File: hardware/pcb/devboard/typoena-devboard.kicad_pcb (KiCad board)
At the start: 4 copper layers, 117 x 45 mm, 86 parts, among them J1 BATTERIE JST-PH, J10 EXTENSION (non monte), J11 DEVKITC-1 rangée gauche, J12 DEVKITC-1 rangée droite, J13 CLAVIER INTERNE, J2 BOUTON contact JST-PH, J3 BOUTON LED JST-PH, J4 FPC 24p 0.5mm - PANNEAU, J5 SECOURS DESPI-C579, J6 USB-C CHARGE + PROG, J7 USB-C CLAVIER (hote), J8 microSD, Q1 AO3401A, Q2 2N7002, Q3 2N7002, Q4 Si1308EDL, SW1 QON, U2 BQ25896RTW, U3 TPS63001DRCR, U4 TPS61023DRL

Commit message: feat(pcb): ready the dev board for fabrication
- drop J10, the unpopulated extension header (schematic + copper)
- extend the In2.Cu +3V3 plane to the left board edge, closing the
  gap under the DevKitC headers, and refill the zones
- mark J11/J12 (DevKitC header rows) DNP for hand-soldering; give J13
  (internal-keyboard JST-PH S4B-PH-K) its LCSC C157926 for fab assembly
- add the dev board BOM source
- gen_fab: apply J13's +180 JLCPCB rotation, matching the other JST-PH
- check_pcb: treat an absent USB pair as not-present, not "unrouted"
  (USB_PROG only exists on the mainboard)

Co-Authored-By: Claude Opus 4.8 <noreply@anthropic.com>
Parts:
- removed J10: EXTENSION (non monte), Connector_PinHeader_2.54mm:PinHeader_1x12_P2.54mm_Vertical
- moved C16 10.5 mm to (23.3, 69.0), turned to 90 degrees
- moved C17 9.12 mm to (21.3, 69.0), turned to 90 degrees
- moved C15 4.60 mm to (22.4, 71.3)
- moved J11 0.40 mm to (19.5, 74.0)
- moved J12 0.40 mm to (19.5, 51.1)
- moved C30 0.30 mm to (33.4, 82.6)
- moved C9 0.30 mm to (36.1, 82.6)
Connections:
- J11 pad 12: IO8 -> unconnected-(J11-Pin_12-Pad12)
- J11 pad 15: IO9 -> unconnected-(J11-Pin_15-Pad15)
- J12 pad 16: IO48 -> unconnected-(J12-Pin_16-Pad16)
- J12 pad 17: IO47 -> unconnected-(J12-Pin_17-Pad17)
- J12 pad 4: IO1 -> unconnected-(J12-Pin_4-Pad4)
- J12 pad 5: IO2 -> unconnected-(J12-Pin_5-Pad5)
- J12 pad 6: IO42 -> unconnected-(J12-Pin_6-Pad6)
- J12 pad 9: IO39 -> unconnected-(J12-Pin_9-Pad9)
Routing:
- net USB_DP: track 5.52 -> 72.3 mm, vias 2 -> 4
- net USB_DM: track 4.29 -> 63.6 mm, vias 2 -> 4
- net SD_SCK: track 1.04 -> 47.6 mm
- net +5V: track 15.9 -> 61.3 mm, vias 4 -> 5
- net SD_MISO: track 6.27 -> 48.9 mm, vias 0 -> 1
- net VBAT: track 4.05 -> 18.0 mm, vias 0 -> 1
- net +3V3: track 47.4 -> 43.5 mm, vias 9 -> 8
- net SD_CS: track 59.8 -> 61.0 mm
- net VSYS: track 119.8 -> 121.0 mm, vias 1 -> 0
- net GND: track 59.0 -> 60.1 mm
- net EPD_SCK: track 102.0 -> 101.0 mm
- net PMIC_INT: track 56.4 -> 55.4 mm
- net EPD_MOSI: track 104.4 -> 103.4 mm
- net SD_MOSI: track 78.7 -> 79.3 mm
- net I2C_SCL: track 52.9 -> 52.4 mm

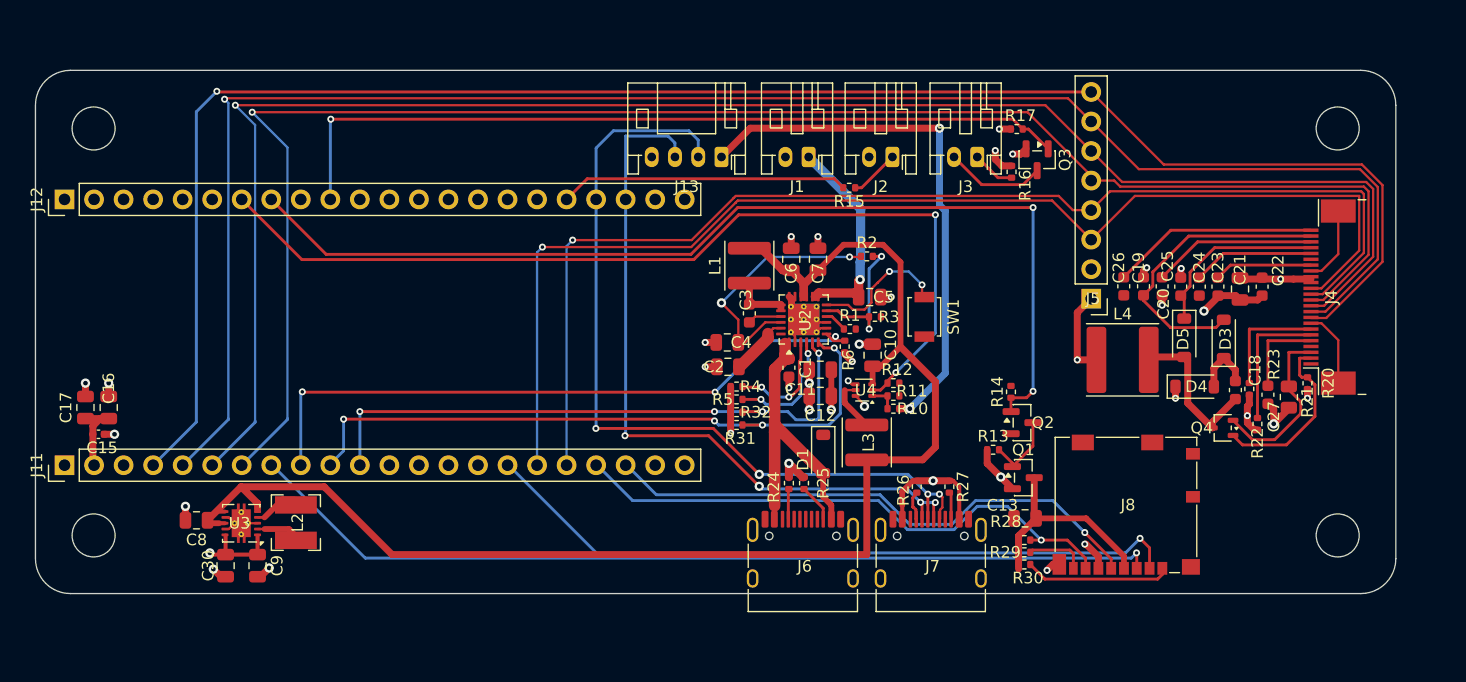
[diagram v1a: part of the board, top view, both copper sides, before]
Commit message: feat(pcb): cost-optimize the dev board for JLCPCB
- shrink the outline to 99 x 45 mm and recenter MH2/MH4, keeping every
  dimension under 100 mm to dodge the large-board engineering fee
- reshape the In2.Cu +5V plane, restore the GND_surface pour, refill zones
- widen the main VBUS run to 1.2 mm, clearing the G2 thermal warning
- mark J1/J2/J3/J13 (JST-PH) and SW1 DNP: hand-soldered, so the board is
  all-SMD and skips the through-hole wave-solder fixture
- move R1/R10/R11/R26/R27 to Basic 0603 (150R/56k/7.5k), dropping three
  extended feeders; values and the 5V feedback ratio preserved
- swap D1 to the promotional SMF5.0A C19077497 (identical part, fee waived)
- gen_fab: J13 takes no JLCPCB rotation correction (verified in preview)

Co-Authored-By: Claude Opus 4.8 <noreply@anthropic.com>
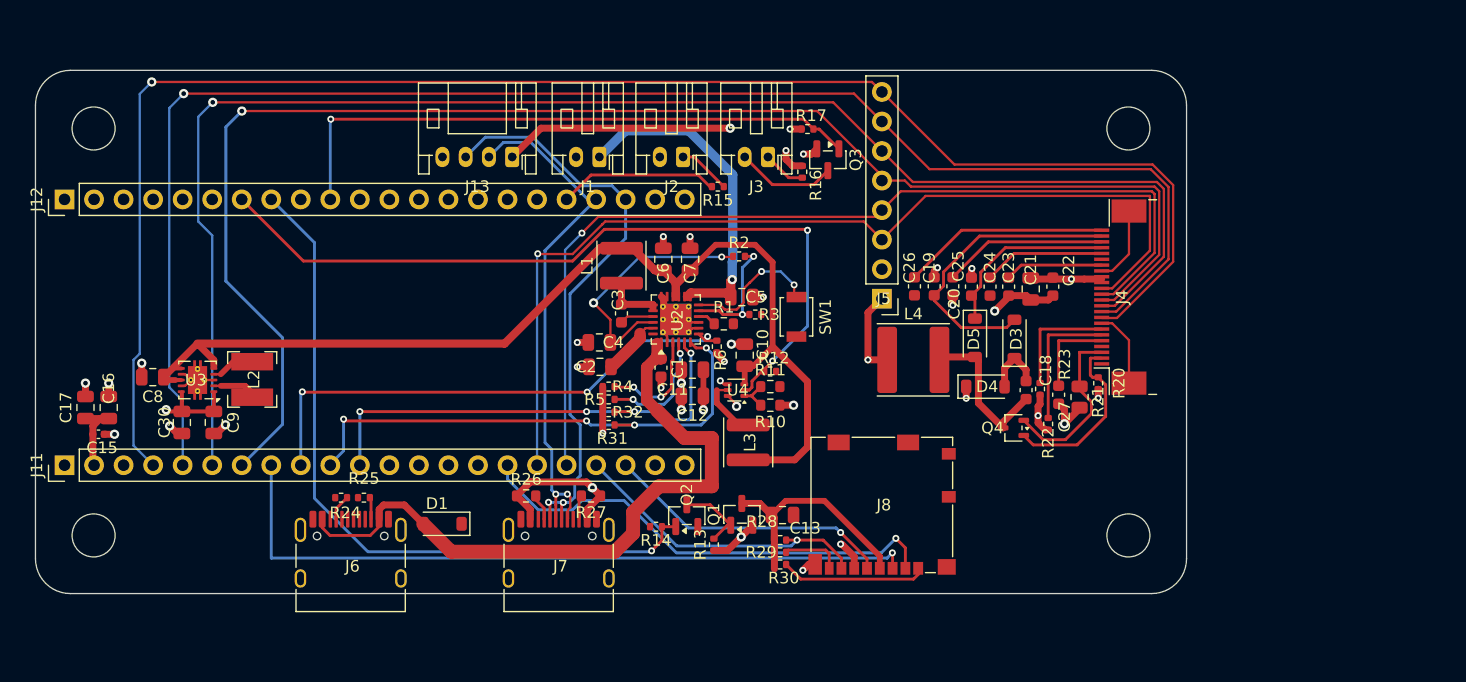
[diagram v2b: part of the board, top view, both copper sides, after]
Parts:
- R1, R10, R11, R26, R27: footprint Resistor_SMD:R_0402_1005Metric -> Resistor_SMD:R_0603_1608Metric
- moved J6 38.9 mm to (44.1, 82.7)
- moved R24 38.5 mm to (43.3, 76.8), turned to 180 degrees
- moved R25 37.9 mm to (45.2, 76.8), turned to 180 degrees
- moved R26 33.6 mm to (59.2, 76.6), turned to 0 degrees
- moved D1 33.3 mm to (52.0, 79.0), turned to 180 degrees
- moved R14 32.7 mm to (70.4, 79.2), turned to 180 degrees
- moved J7 32.0 mm to (62.0, 82.7)
- moved R27 30.8 mm to (64.8, 76.6), turned to 180 degrees
- moved Q2 29.9 mm to (73.0, 78.3), turned to 90 degrees
- moved R13 25.4 mm to (75.3, 80.8), turned to 90 degrees
- moved Q1 24.4 mm to (77.8, 78.2), turned to 90 degrees
- moved J8 21.0 mm to (89.8, 77.4)
- moved R28 21.0 mm to (81.0, 80.4)
- moved R29 21.0 mm to (81.0, 81.5)
- moved R30 21.0 mm to (81.0, 82.5)
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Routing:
- net VBUS: track 25.6 -> 58.6 mm
- net USB_DP: track 72.3 -> 44.8 mm, vias 4 -> 2
- net SD_PWR_EN: track 88.3 -> 61.8 mm, vias 2 -> 1
- net VSYS: track 121.0 -> 95.7 mm
- net SD_SCK: track 47.6 -> 24.9 mm
- net +5V: track 61.3 -> 38.8 mm
- net SD_MISO: track 48.9 -> 26.6 mm
- net SD_CS: track 61.0 -> 41.3 mm
- net EPD_MOSI: track 103.4 -> 84.4 mm
- net EPD_SCK: track 101.0 -> 82.5 mm
- net BTN_LED: track 70.1 -> 52.1 mm
- net EPD_DC: track 147.0 -> 130.0 mm
- net SD_MOSI: track 79.3 -> 63.0 mm
- net EPD_CS: track 144.3 -> 128.5 mm
- net EPD_RST: track 149.4 -> 134.8 mm
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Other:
- board size 117 x 45 mm -> 99 x 45 mm

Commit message: fix(pcb): turn the VBUS TVS the right way round on both boards
D1 (SMF5.0A, unidirectional) carried Device:D_TVS, KiCad's bidirectional
symbol. Its pins are A1/A2, so no polarity is expressed, ERC has nothing to
reject, and the cathode landed wherever the wire ran — on GND. Plugging in
USB-C would have forward-biased the diode straight across VBUS, shorting the
port it protects.

Both boards now use Device:D_Zener, pin 1 = K, cathode on VBUS. The footprint
is rotated 180° so the symmetric SOD-123 pads keep the same copper: no track
moves, and DRC and unconnected counts are identical before and after.

check_pcb.py gains control H3 — every D<n> footprint must carry K/A pads. It
fails on the boards as they stood and passes 4/4 on the corrected ones.

Co-Authored-By: Claude Opus 5 (1M context) <noreply@anthropic.com>
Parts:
- turned D1 to 0 degrees
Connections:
- D1 pad 1: GND -> VBUS
- D1 pad 2: VBUS -> GND
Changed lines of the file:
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@@
 	(footprint "Diode_SMD:D_SOD-123"
 		(layer "F.Cu")
-		(at 52 79 180)
+		(at 52 79)
 		(descr "SOD-123")
 		(tags "SOD-123")
 		(property "Reference" "D1"
-			(at 0.4659 1.7387 0)
+			(at 0.4659 1.7387 180)
 			(layer "F.SilkS")
 			(effects
@@
 		)
 		(property "Value" "SMF5.0A"
-			(at 0 2.1 0)
+			(at 0 2.1 180)
 			(layer "F.Fab")
 			(effects
@@
 		)
 		(property "Datasheet" ""
-			(at 0 0 180)
+			(at 0 0 0)
 			(unlocked yes)
 			(layer "F.Fab")
@@
 		)
 		(property "Description" ""
-			(at 0 0 180)
+			(at 0 0 0)
 			(unlocked yes)
 			(layer "F.Fab")
@@
 		)
 		(property "LCSC" "C284108"
-			(at 0 0 180)
+			(at 0 0 0)
 			(unlocked yes)
 			(layer "F.Fab")
@@
 		)
 		(property "MPN" "SMF5.0A"
-			(at 0 0 180)
+			(at 0 0 0)
 			(unlocked yes)
 			(layer "F.Fab")
@@
 		(duplicate_pad_numbers_are_jumpers no)
 		(fp_line
+			(start -2.36 -1)
+			(end -2.36 1)
+			(stroke
+				(width 0.12)
+				(type solid)
+			)
+			(layer "F.SilkS")
+		)
+		(fp_line
+			(start -2.36 -1)
+			(end 1.65 -1)
+			(stroke
+				(width 0.12)
+				(type solid)
+			)
+			(layer "F.SilkS")
+		)
+		(fp_line
 			(start -2.36 1)
 			(end 1.65 1)
@@
 		)
 		(fp_line
-			(start -2.36 -1)
-			(end 1.65 -1)
-			(stroke
-				(width 0.12)
-				(type solid)
-			)
-			(layer "F.SilkS")
-		)
-		(fp_line
-			(start -2.36 -1)
-			(end -2.36 1)
-			(stroke
-				(width 0.12)
-				(type solid)
-			)
-			(layer "F.SilkS")
+			(start -2.35 -1.15)
+			(end -2.35 1.15)
+			(stroke
+				(width 0.05)
+				(type solid)
+			)
+			(layer "F.CrtYd")
+		)
+		(fp_line
+			(start -2.35 -1.15)
+			(end 2.35 -1.15)
+			(stroke
+				(width 0.05)
+				(type solid)
+			)
+			(layer "F.CrtYd")
+		)
+		(fp_line
+			(start 2.35 -1.15)
+			(end 2.35 1.15)
+			(stroke
+				(width 0.05)
+				(type solid)
+			)
+			(layer "F.CrtYd")
 		)
 		(fp_line
@@
 		)
 		(fp_line
-			(start 2.35 -1.15)
-			(end 2.35 1.15)
-			(stroke
-				(width 0.05)
-				(type solid)
-			)
-			(layer "F.CrtYd")
-		)
-		(fp_line
-			(start -2.35 -1.15)
-			(end 2.35 -1.15)
-			(stroke
-				(width 0.05)
-				(type solid)
-			)
-			(layer "F.CrtYd")
-		)
-		(fp_line
-			(start -2.35 -1.15)
-			(end -2.35 1.15)
-			(stroke
-				(width 0.05)
-				(type solid)
-			)
-			(layer "F.CrtYd")
+			(start -1.4 -0.9)
+			(end 1.4 -0.9)
+			(stroke
+				(width 0.1)
+				(type solid)
+			)
+			(layer "F.Fab")
+		)
+		(fp_line
+			(start -1.4 0.9)
+			(end -1.4 -0.9)
+			(stroke
+				(width 0.1)
+				(type solid)
+			)
+			(layer "F.Fab")
+		)
+		(fp_line
+			(start -0.75 0)
+			(end -0.35 0)
+			(stroke
+				(width 0.1)
+				(type solid)
+			)
+			(layer "F.Fab")
+		)
+		(fp_line
+			(start -0.35 0)
+			(end -0.35 -0.55)
+			(stroke
+				(width 0.1)
+				(type solid)
+			)
+			(layer "F.Fab")
+		)
+		(fp_line
+			(start -0.35 0)
+			(end -0.35 0.55)
+			(stroke
+				(width 0.1)
+				(type solid)
+			)
+			(layer "F.Fab")
+		)
+		(fp_line
+			(start -0.35 0)
+			(end 0.25 -0.4)
+			(stroke
+				(width 0.1)
+				(type solid)
+			)
+			(layer "F.Fab")
+		)
+		(fp_line
+			(start 0.25 -0.4)
+			(end 0.25 0.4)
+			(stroke
+				(width 0.1)
+				(type solid)
+			)
+			(layer "F.Fab")
+		)
+		(fp_line
+			(start 0.25 0)
+			(end 0.75 0)
+			(stroke
+				(width 0.1)
+				(type solid)
+			)
+			(layer "F.Fab")
+		)
+		(fp_line
+			(start 0.25 0.4)
+			(end -0.35 0)
+			(stroke
+				(width 0.1)
+				(type solid)
+			)
+			(layer "F.Fab")
+		)
+		(fp_line
+			(start 1.4 -0.9)
+			(end 1.4 0.9)
+			(stroke
+				(width 0.1)
+				(type solid)
+			)
+			(layer "F.Fab")
 		)
 		(fp_line
@@
 			(layer "F.Fab")
 		)
-		(fp_line
-			(start 1.4 -0.9)
-			(end 1.4 0.9)
-			(stroke
-				(width 0.1)
-				(type solid)
-			)
-			(layer "F.Fab")
-		)
-		(fp_line
-			(start 0.25 0.4)
-			(end -0.35 0)
-			(stroke
-				(width 0.1)
-				(type solid)
-			)
-			(layer "F.Fab")
-		)
-		(fp_line
-			(start 0.25 0)
-			(end 0.75 0)
-			(stroke
-				(width 0.1)
-				(type solid)
-			)
-			(layer "F.Fab")
-		)
-		(fp_line
-			(start 0.25 -0.4)
-			(end 0.25 0.4)
-			(stroke
-				(width 0.1)
-				(type solid)
-			)
-			(layer "F.Fab")
-		)
-		(fp_line
-			(start -0.35 0)
-			(end 0.25 -0.4)
-			(stroke
-				(width 0.1)
-				(type solid)
-			)
-			(layer "F.Fab")
-		)
-		(fp_line
-			(start -0.35 0)
-			(end -0.35 0.55)
-			(stroke
-				(width 0.1)
-				(type solid)
-			)
-			(layer "F.Fab")
-		)
-		(fp_line
-			(start -0.35 0)
-			(end -0.35 -0.55)
-			(stroke
-				(width 0.1)
-				(type solid)
-			)
-			(layer "F.Fab")
-		)
-		(fp_line
-			(start -0.75 0)
-			(end -0.35 0)
-			(stroke
-				(width 0.1)
-				(type solid)
-			)
-			(layer "F.Fab")
-		)
-		(fp_line
-			(start -1.4 0.9)
-			(end -1.4 -0.9)
-			(stroke
-				(width 0.1)
-				(type solid)
-			)
-			(layer "F.Fab")
-		)
-		(fp_line
-			(start -1.4 -0.9)
-			(end 1.4 -0.9)
-			(stroke
-				(width 0.1)
-				(type solid)
-			)
-			(layer "F.Fab")
-		)
 		(fp_text user "${REFERENCE}"
-			(at 0 -2 0)
+			(at 0 -2 180)
 			(layer "F.Fab")
 			(effects
@@
 		)
 		(pad "1" smd roundrect
-			(at -1.65 0 180)
+			(at -1.65 0)
+			(size 0.9 1.2)
+			(layers "F.Cu" "F.Mask" "F.Paste")
+			(roundrect_rratio 0.25)
+			(net "VBUS")
+			(pinfunction "K_1")
+			(pintype "passive")
+		)
+		(pad "2" smd roundrect
+			(at 1.65 0)
 			(size 0.9 1.2)
 			(layers "F.Cu" "F.Mask" "F.Paste")
 			(roundrect_rratio 0.25)
 			(net "GND")
-			(pinfunction "A1_1")
+			(pinfunction "A_2")
 			(pintype "passive")
 		)
-		(pad "2" smd roundrect
-			(at 1.65 0 180)
-			(size 0.9 1.2)
-			(layers "F.Cu" "F.Mask" "F.Paste")
-			(roundrect_rratio 0.25)
-			(net "VBUS")
-			(pinfunction "A2_2")
-			(pintype "passive")
-		)
